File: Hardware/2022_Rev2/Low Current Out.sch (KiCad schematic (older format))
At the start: 81 parts

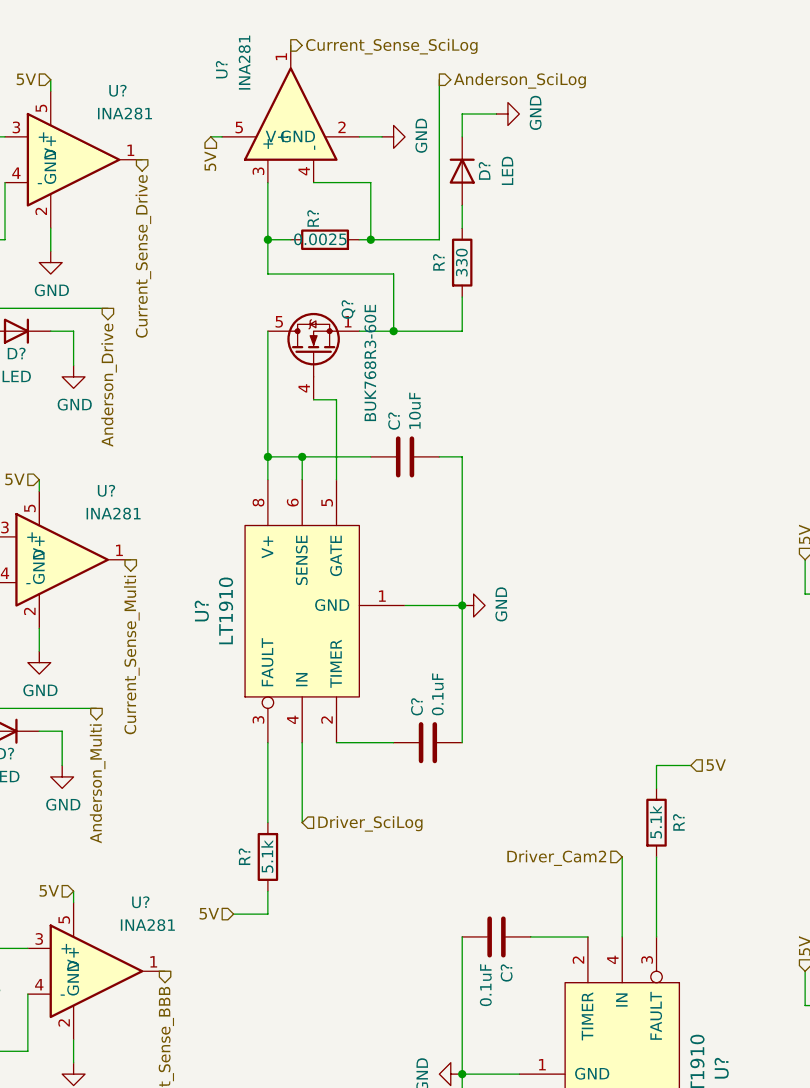
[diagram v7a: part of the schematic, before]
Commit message: removed scilog/sciact
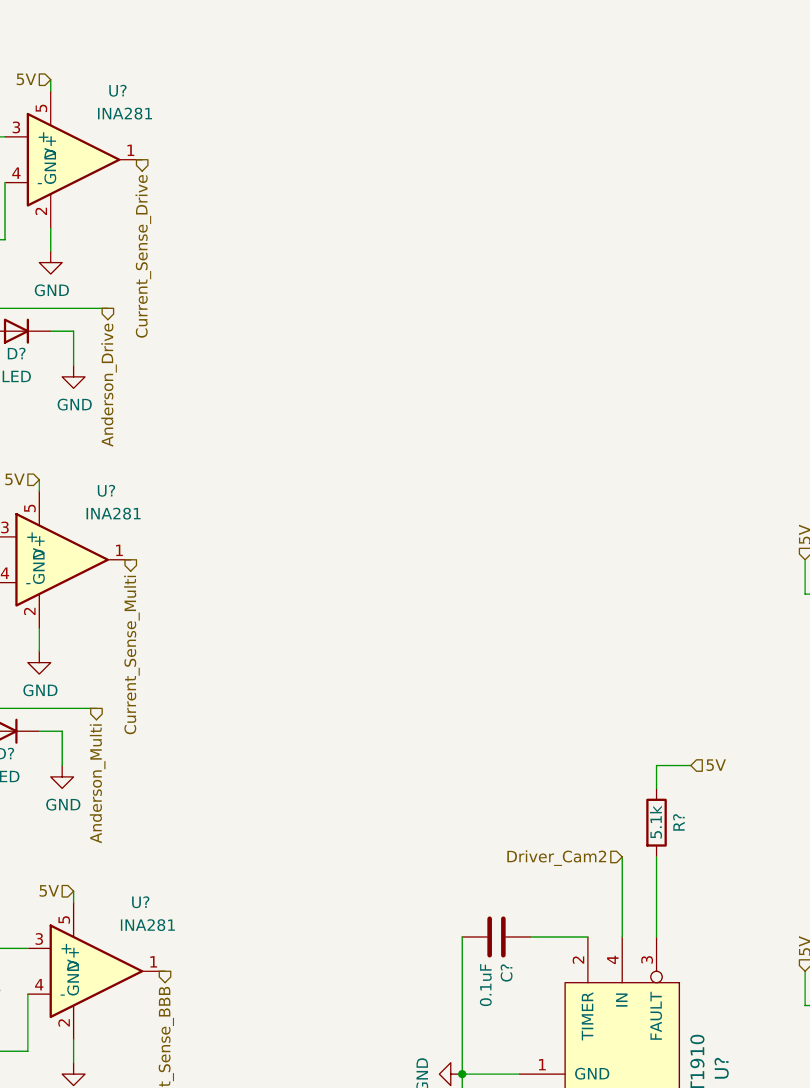
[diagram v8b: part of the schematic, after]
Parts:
- removed C?: 0.1uF, symbol Device:C
- removed C?: 10uF, symbol Device:C
- removed D?: LED, symbol Device:D
- removed Q?: BUK768R3-60E, Package_TO_SOT_SMD:LFPAK33, symbol Transistor_FET:BUK7M9R9-60EX
- removed R?: 5.1k, symbol Device:R
- removed R?: 330, symbol Device:R
- removed R?: 0.0025, symbol Device:R
- removed U?: LT1910, symbol 2022_Rev2-rescue:LT1910-MRDT_ICs
- removed U?: INA281, Package_TO_SOT_SMD:SOT-23-5, symbol 2022_Rev2-rescue:INA281-MRDT_ICs
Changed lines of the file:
@@
-$Comp
-L Device:R R?
-U 1 1 623AA14E
-P 4900 4250
-F 0 "R?" V 5000 4250 50  0000 C CNN
-F 1 "5.1k" V 4900 4250 50  0000 C CNN
-F 2 "" V 4830 4250 50  0001 C CNN
-F 3 "~" H 4900 4250 50  0001 C CNN
-	1    4900 4250
-	-1   0    0    1
-$EndComp
-$Comp
-L 2022_Rev2-rescue:LT1910-MRDT_ICs U?
-U 1 1 623AA154
-P 5300 3550
-F 0 "U?" H 5675 4237 60  0000 C CNN
-F 1 "LT1910" H 5675 4131 60  0000 C CNN
-F 2 "" H 5300 3550 60  0001 C CNN
-F 3 "" H 5300 3550 60  0001 C CNN
-	1    5300 3550
-	0    -1   -1   0
-$EndComp
-$Comp
-L Device:C C?
-U 1 1 623AA15A
-P 5600 3750
-F 0 "C?" H 5715 3796 50  0000 L CNN
-F 1 "0.1uF" H 5715 3705 50  0000 L CNN
-F 2 "" H 5638 3600 50  0001 C CNN
-F 3 "~" H 5600 3750 50  0001 C CNN
-	1    5600 3750
-	0    -1   -1   0
-$EndComp
-$Comp
-L power:GND #PWR?
-U 1 1 623AA160
-P 5750 3150
-F 0 "#PWR?" H 5750 2900 50  0001 C CNN
-F 1 "GND" H 5755 2977 50  0000 C CNN
-F 2 "" H 5750 3150 50  0001 C CNN
-F 3 "" H 5750 3150 50  0001 C CNN
-	1    5750 3150
-	0    -1   -1   0
-$EndComp
-$Comp
-L Device:C C?
-U 1 1 623AA166
-P 5500 2500
-F 0 "C?" H 5615 2546 50  0000 L CNN
-F 1 "10uF" H 5615 2455 50  0000 L CNN
-F 2 "" H 5538 2350 50  0001 C CNN
-F 3 "~" H 5500 2500 50  0001 C CNN
-	1    5500 2500
-	0    -1   -1   0
-$EndComp
-$Comp
-L Transistor_FET:BUK7M9R9-60EX Q?
-U 1 1 623AA16C
-P 5100 2050
-F 0 "Q?" H 5250 1900 50  0000 L CNN
-F 1 "BUK768R3-60E" H 4800 1800 50  0000 L CNN
-F 2 "Package_TO_SOT_SMD:LFPAK33" H 5300 1975 50  0001 L CIN
-F 3 "https://assets.nexperia.com/documents/data-sheet/BUK7M9R9-60E.pdf" V 5100 2050 50  0001 L CNN
-	1    5100 2050
-	0    -1   -1   0
-$EndComp
-$Comp
-L Device:R R?
-U 1 1 623AA172
-P 5750 1650
-F 0 "R?" V 5650 1650 50  0000 C CNN
-F 1 "330" V 5750 1650 50  0000 C CNN
-F 2 "" V 5680 1650 50  0001 C CNN
-F 3 "~" H 5750 1650 50  0001 C CNN
-	1    5750 1650
-	1    0    0    -1
-$EndComp
-$Comp
-L Device:D D?
-U 1 1 623AA178
-P 5750 1250
-F 0 "D?" H 5750 1350 50  0000 C CNN
-F 1 "LED" H 5750 1450 50  0000 C CNN
-F 2 "" H 5750 1250 50  0001 C CNN
-F 3 "~" H 5750 1250 50  0001 C CNN
-	1    5750 1250
-	0    1    1    0
-$EndComp
-$Comp
-L 2022_Rev2-rescue:INA281-MRDT_ICs U?
-U 1 1 623AA17E
-P 5000 1100
-F 0 "U?" H 5250 1400 50  0000 L CNN
-F 1 "INA281" H 5200 1300 50  0000 L CNN
-F 2 "Package_TO_SOT_SMD:SOT-23-5" H 5250 1300 50  0001 C CNN
-F 3 "https://www.ti.com/lit/ds/symlink/ina281.pdf?ts=1602621825218&ref_url=https%253A%252F%252Fwww.ti.com%252Fproduct%252FINA281" H 5250 1300 50  0001 C CNN
-	1    5000 1100
-	0    -1   -1   0
-$EndComp
-Wire Wire Line
-	4900 4100 4900 3750
-Wire Wire Line
-	5050 3750 5050 4100
-Wire Wire Line
-	5200 3750 5450 3750
-Wire Wire Line
-	5750 3750 5750 3150
-Wire Wire Line
-	5500 3150 5750 3150
-Connection ~ 5750 3150
-Wire Wire Line
-	5750 3150 5750 2500
-Wire Wire Line
-	5750 2500 5650 2500
-Wire Wire Line
-	5350 2500 5050 2500
-Wire Wire Line
-	5050 2500 5050 2600
-Wire Wire Line
-	4900 2600 4900 2500
-Wire Wire Line
-	4900 2500 5050 2500
-Connection ~ 5050 2500
-Wire Wire Line
-	5100 2250 5200 2250
-Wire Wire Line
-	5200 2250 5200 2600
-Wire Wire Line
-	4900 2500 4900 1950
-Connection ~ 4900 2500
-Wire Wire Line
-	5300 1950 5450 1950
-Wire Wire Line
-	5750 1950 5750 1800
-Wire Wire Line
-	5750 1500 5750 1400
-Wire Wire Line
-	5750 1100 5750 1000
-Wire Wire Line
-	5750 1000 5900 1000
-$Comp
-L power:GND #PWR?
-U 1 1 623AA19A
-P 5900 1000
-F 0 "#PWR?" H 5900 750 50  0001 C CNN
-F 1 "GND" H 5905 827 50  0000 C CNN
-F 2 "" H 5900 1000 50  0001 C CNN
-F 3 "" H 5900 1000 50  0001 C CNN
-	1    5900 1000
-	0    -1   -1   0
-$EndComp
-$Comp
-L Device:R R?
-U 1 1 623AA1A0
-P 5150 1550
-F 0 "R?" H 5200 1600 50  0000 L CNN
-F 1 "0.0025" V 5150 1450 50  0000 L CNN
-F 2 "" V 5080 1550 50  0001 C CNN
-F 3 "~" H 5150 1550 50  0001 C CNN
-	1    5150 1550
-	0    -1   -1   0
-$EndComp
-Wire Wire Line
-	5450 1950 5450 1700
-Wire Wire Line
-	5450 1700 4900 1700
-Wire Wire Line
-	4900 1700 4900 1550
-Connection ~ 5450 1950
-Wire Wire Line
-	5450 1950 5750 1950
-Wire Wire Line
-	4900 1550 5000 1550
-Connection ~ 4900 1550
-Wire Wire Line
-	4900 1550 4900 1300
-Wire Wire Line
-	5300 1550 5350 1550
-Wire Wire Line
-	5350 1550 5350 1300
-Wire Wire Line
-	5350 1300 5100 1300
-Connection ~ 5350 1550
-$Comp
-L power:GND #PWR?
-U 1 1 623AA1B2
-P 5400 1100
-F 0 "#PWR?" H 5400 850 50  0001 C CNN
-F 1 "GND" H 5405 927 50  0000 C CNN
-F 2 "" H 5400 1100 50  0001 C CNN
-F 3 "" H 5400 1100 50  0001 C CNN
-	1    5400 1100
-	0    -1   -1   0
-$EndComp
-Wire Wire Line
-	5350 1550 5650 1550
-Wire Wire Line
-	5300 1100 5400 1100
-Wire Wire Line
-	4700 1100 4650 1100
-Text HLabel 5000 700  2    50   Output ~ 0
-Current_Sense_SciLog
-Text HLabel 5650 850  2    50   Output ~ 0
-Anderson_SciLog
-Wire Wire Line
-	5650 1550 5650 850
-Wire Wire Line
-	4900 4400 4900 4500
-Wire Wire Line
-	4900 4500 4750 4500
-Text HLabel 5050 4100 2    50   Input ~ 0
-Driver_SciLog
-Text HLabel 4750 4500 0    50   Input ~ 0
-5V
-Text HLabel 4650 1100 3    50   Input ~ 0
-5V
 $Comp
 L Device:R R?
